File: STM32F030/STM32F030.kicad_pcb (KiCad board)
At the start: 4 copper layers, 88.9 x 69.1 mm, 46 parts, among them J1 USB_OTG, J4 I2C, J5 SWD, J6 SPI, J7 UART, J8 MCP2200 GPIO, J9 analog pins, SW1 NRST, SW2 BOOT0, U1 STM32F030RCTx, U2 MCP2200T-I-SO, U3 AZ1117-3.3, Y1 16MHz, Y2 12MHz

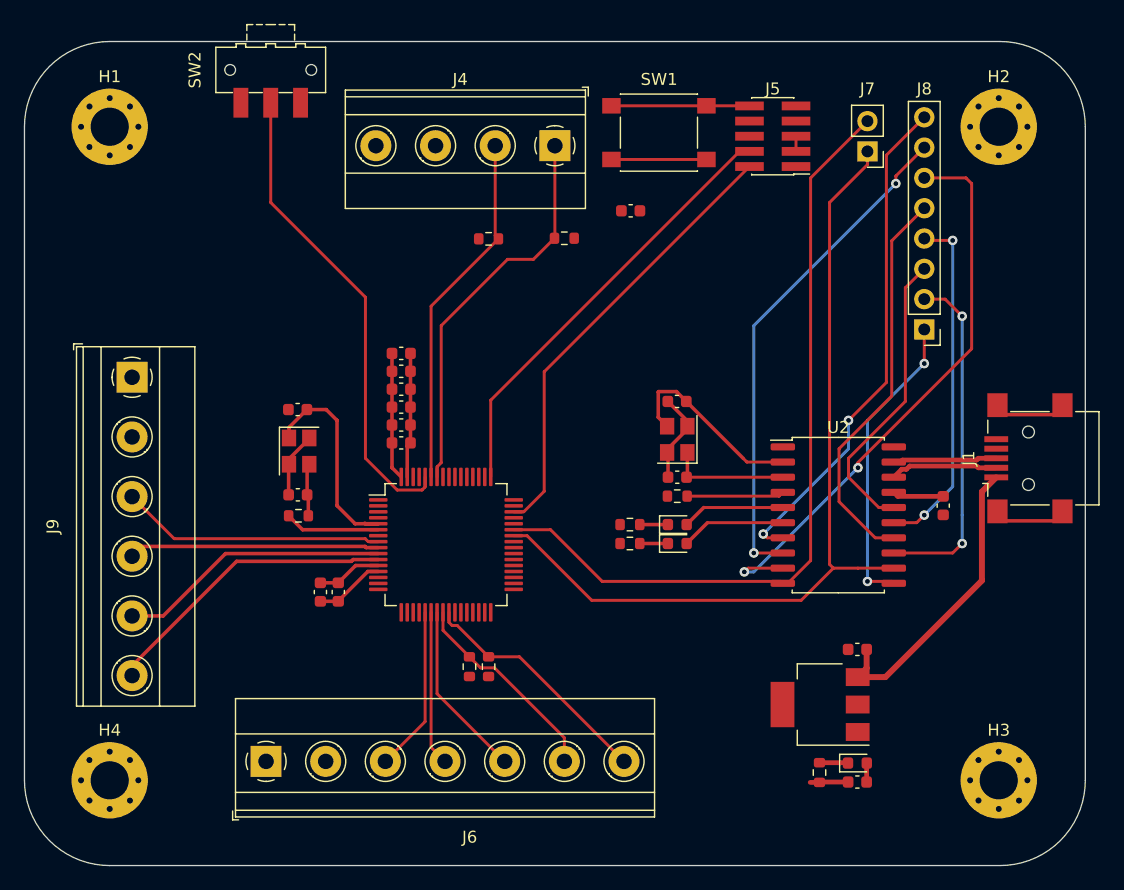
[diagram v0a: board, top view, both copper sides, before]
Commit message: finished the PCB just need to double check everything is good
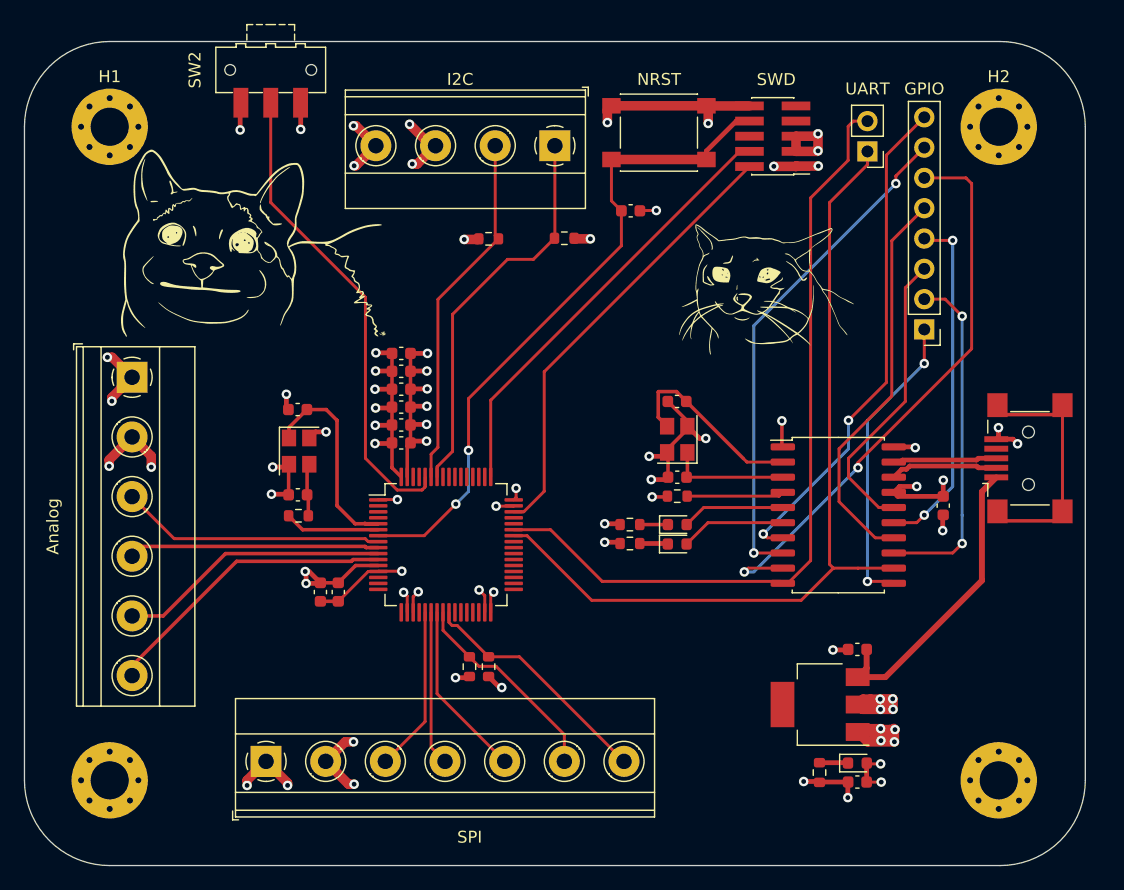
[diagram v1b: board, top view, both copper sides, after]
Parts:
- added G***: LOGO, LOGO, F.Cu at (114.2, 75.8)
- added G***: LOGO, LOGO, F.Cu at (157.4, 79.8)
- renumbered J9 to Analog, J8 to GPIO, J4 to I2C, SW1 to NRST, J6 to SPI, J5 to SWD, J7 to UART
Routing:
- net GND: track 46.4 -> 128.8 mm, vias 0 -> 43
- net +3.3V: track 22.4 -> 88.8 mm, vias 0 -> 34
- net NRST: track 7.96 -> 55.9 mm, vias 0 -> 2
- net unconnected-(J1-Shield-Pad6): track 10.9 -> 19.8 mm
- net USART1_RX: track 66.8 -> 67.5 mm
- added copper zone on In1.Cu, net +3.3V
- added copper zone on In2.Cu, net GND
